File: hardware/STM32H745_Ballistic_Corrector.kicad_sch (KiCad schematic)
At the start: 0 parts

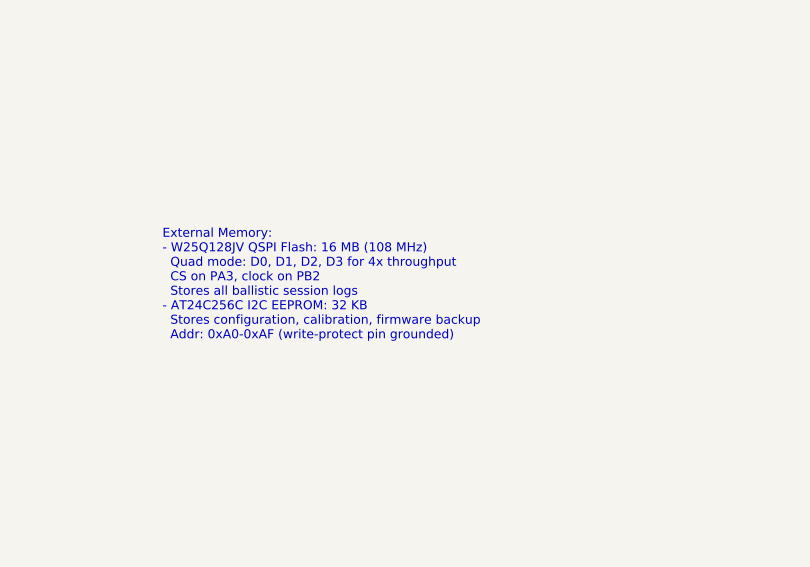
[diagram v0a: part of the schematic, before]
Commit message: Add board integration HLD + KiCad PCB project skeleton
HLD (hardware/HLD_BOARD_INTEGRATION.md):
- Platform comparison and decision: STM32H745 stays for v1.x (critical
  path, Gerber lock 2026-08-11); STM32N6 recommended for v2.0 edge-AI
  variant (M55 + Neural-ART 600 GOPS @ 3 TOPS/W, 4.2 MB SRAM, same
  real-time class); STM32MP2 rejected (Linux latency, DDR/PMIC board
  complexity, 2-10 s boot, power budget)
- System context diagram, power tree, pin map, IPC memory map
- v1.x -> v2.0 drop-in compatibility strategy: fixed 80x60 mm outline,
  M3 hole positions, 14-pin sensor connector pinout, 12 V input
- PCB plan: 4-layer stackup with impedance targets, netclass table,
  placement floorplan, 10-step routing work order (~46 h to Gerber lock)

KiCad project started (attached to existing schematic):
- .kicad_pro: 7 netclasses (QSPI_50R 0.28mm, USB_90R diff, I2C, SPI,
  power classes), DRC minimums, track/via tables
- .kicad_pcb: 4-layer stackup (7628 prepreg, ENIG), 80x60 mm outline
  with R2 corners, 4x M3 mounting holes tied to GND, solid In1 GND
  plane, In2 power pours (5V/3V3 split), B.Cu GND pour, floorplan
  placement zones and QSPI routing notes on user layers
- .kicad_dru: custom rules - QSPI width lock and outer-layer-only
  routing, USB diff geometry, 12V clearance, power via size

Schematic fix: QSPI_CS pin conflict resolved - PA3 was double-assigned
to USART2_RX; QSPI BK1_NCS moved to PB6 (AF10), full QSPI pin mapping
documented (D0=PD11, D1=PD12, D2=PE2, D3=PD13)

Co-Authored-By: Claude Fable 5 <noreply@anthropic.com>
Claude-Session: https://claude.ai/code/session_01WTnjtLhvvQkSSzjNBr8Vvw
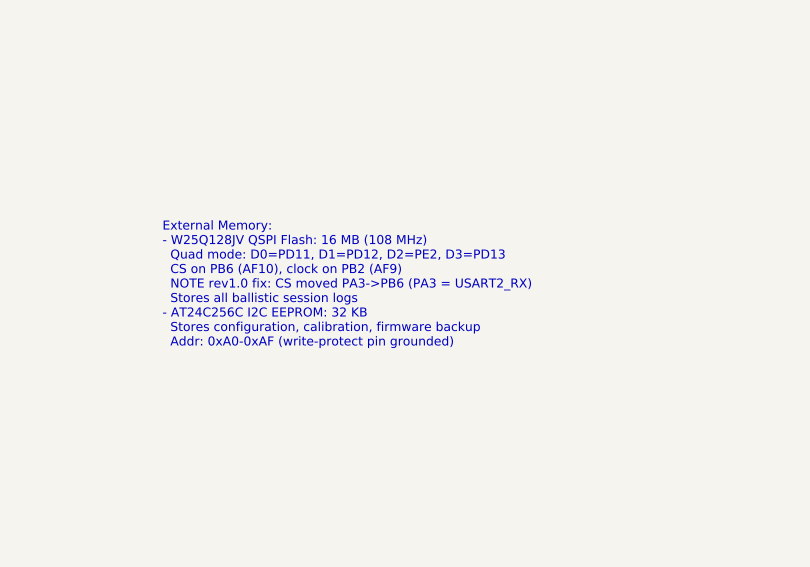
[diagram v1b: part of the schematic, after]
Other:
- note added: "External Memory: - W25Q128JV QSPI Flash: 16 MB (108 MHz) Quad mode: D0=PD11, D1=PD12, D2=PE2, D3=PD13 CS on PB6 (AF10), clock on PB2 (AF9) NOTE rev1.0 fix: CS moved PA3->PB6 (PA3 = USART2_RX) Stores all ballistic session logs - AT24C256C I2C EEPROM: 32 KB Stores configuration, calibration, firmware backup Addr: 0xA0-0xAF (write-protect pin grounded)"
- note removed: "External Memory: - W25Q128JV QSPI Flash: 16 MB (108 MHz) Quad mode: D0, D1, D2, D3 for 4x throughput CS on PA3, clock on PB2 Stores all ballistic session logs - AT24C256C I2C EEPROM: 32 KB Stores configuration, calibration, firmware backup Addr: 0xA0-0xAF (write-protect pin grounded)"
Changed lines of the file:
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@@
     (uuid "sensor-annotation")
   )
-  (text "External Memory:\n- W25Q128JV QSPI Flash: 16 MB (108 MHz)\n  Quad mode: D0, D1, D2, D3 for 4x throughput\n  CS on PA3, clock on PB2\n  Stores all ballistic session logs\n- AT24C256C I2C EEPROM: 32 KB\n  Stores configuration, calibration, firmware backup\n  Addr: 0xA0-0xAF (write-protect pin grounded)" (at 150 560 0)
+  (text "External Memory:\n- W25Q128JV QSPI Flash: 16 MB (108 MHz)\n  Quad mode: D0=PD11, D1=PD12, D2=PE2, D3=PD13\n  CS on PB6 (AF10), clock on PB2 (AF9)\n  NOTE rev1.0 fix: CS moved PA3->PB6 (PA3 = USART2_RX)\n  Stores all ballistic session logs\n- AT24C256C I2C EEPROM: 32 KB\n  Stores configuration, calibration, firmware backup\n  Addr: 0xA0-0xAF (write-protect pin grounded)" (at 150 560 0)
     (effects (font (size 1 1) (thickness 0.15)) (justify left))
     (uuid "memory-annotation")
